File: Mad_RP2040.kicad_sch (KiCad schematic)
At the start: 22 parts, among them J1 USB_C_Receptacle, SW1 SW_SPST, SW2 SW_SPST, U0 PCB, U1 ECMF02-2AMX6

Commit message: BOM update
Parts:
- C1, C2: LCSC PN (none) -> C432917
- C3: LCSC PN (none) -> C472857
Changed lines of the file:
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@@
+			)
+		)
+		(property "LCSC PN" "C472857"
+			(at 104.14 39.37 0)
+			(effects
+				(font
+					(size 1.27 1.27)
+				)
+				(hide yes)
 			)
 		)
@@
 			)
 		)
+		(property "LCSC PN" "C432917"
+			(at 66.04 39.37 0)
+			(effects
+				(font
+					(size 1.27 1.27)
+				)
+				(hide yes)
+			)
+		)
 		(pin "2"
 		)
@@
 			(at 87.63 39.37 0)
 			(effects
+				(font
+					(size 1.27 1.27)
+				)
+				(hide yes)
+			)
+		)
+		(property "LCSC PN" "C432917"
+			(at 87.63 39.37 0)
+			(effects

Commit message: BOM consolidation
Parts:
- added D9: B5817WS, Diode_SMD:D_SOD-323, symbol Device:D_Schottky
- added F1: 500mA, Fuse:Fuse_0402_1005Metric, symbol Device:Polyfuse_Small
- C3: LCSC PN C472857 -> C2932476
- FB1: value BLM15PX330SN1D -> 33 Ohms Ferrite
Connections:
- net +5V: now also D9.1 (K); no longer FB1.2
- new net: D9.2 (A), F1.1
- new net: F1.2, FB1.2
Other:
- moved on the sheet: C2, C3

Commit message: BOM update
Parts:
- C1, C2: LCSC (none) -> C432917; LCSC PN C432917 -> (none)
- C3: LCSC (none) -> C2932476; LCSC PN C2932476 -> (none)
- D1, D2: LCSC (none) -> C435829; LCSC PN C435829 -> (none)
- D3, D4: LCSC (none) -> C5149201; LCSC PN C5149201 -> (none)
- D8: LCSC (none) -> C2886570; LCSC PN C2886570 -> (none)
- D9: LCSC (none) -> C122854; LCSC PN C122854 -> (none)
- F1: LCSC (none) -> C206938; LCSC PN C206938 -> (none)
- FB1, FB2: LCSC (none) -> C160974; LCSC PN C160974 -> (none)
- J1: LCSC (none) -> C3020560; LCSC PN C3020560 -> (none)
- R1, R2: LCSC (none) -> C105872; LCSC PN C105872 -> (none)
- SW1, SW2: LCSC (none) -> C2803348; LCSC PN C2803348 -> (none)
- U1: LCSC (none) -> C2651144; LCSC PN C2651144 -> (none)
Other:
- moved on the sheet: C2, C3, D9, F1

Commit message: Update todo's
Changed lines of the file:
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@@
-		)
-	)
-	(text_box "TODO:\n\n#* Cleanup bom, remove trailing spaces\n#* Get missing 3D models\n* Finish off PCB routing\n#* Check LED selection\n* BOM consolidation if possible\n#* Create template for page title block"
-		(exclude_from_sim no)
-		(at 151.765 -34.925 0)
-		(size 132.715 45.72)
-		(stroke
-			(width 0)
-			(type default)
-		)
-		(fill
-			(type none)
-		)
-		(effects
-			(font
-				(size 3 3)
-				(thickness 0.6)
-				(bold yes)
-			)
-			(justify left top)
 		)
 	)

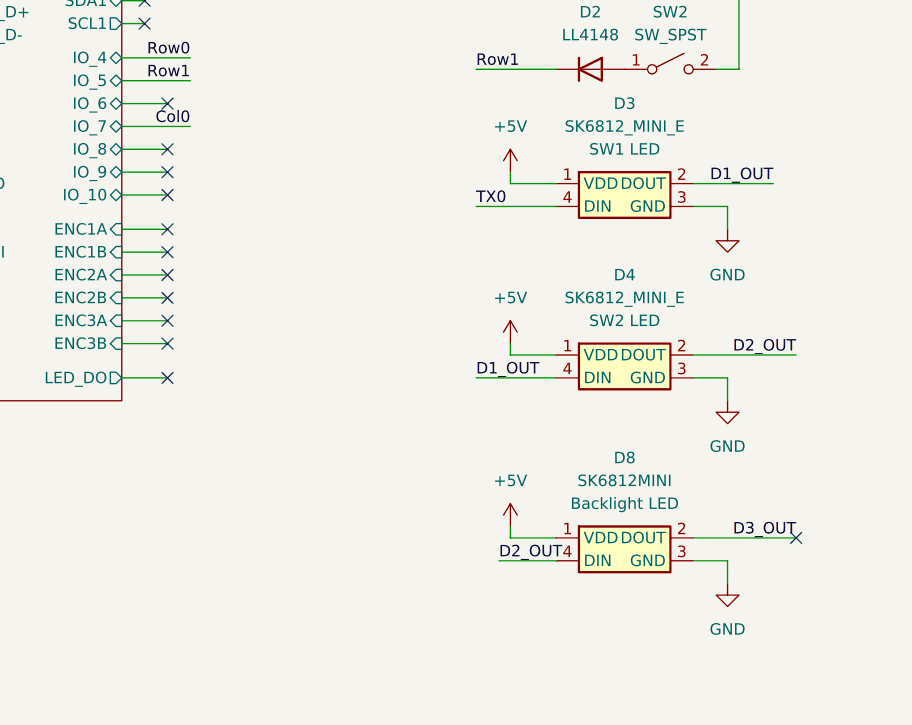
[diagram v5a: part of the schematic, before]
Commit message: Minor silk update
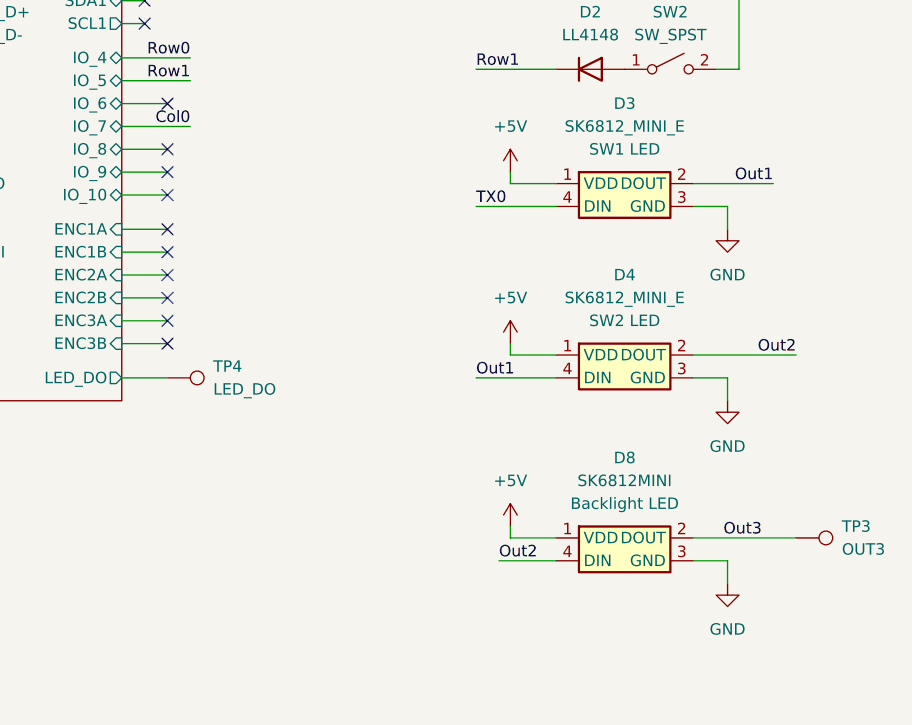
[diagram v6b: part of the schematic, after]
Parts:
- added TP3: OUT3, TestPoint:TestPoint_Pad_D1.0mm, symbol Connector:TestPoint
- added TP4: LED_DO, TestPoint:TestPoint_Pad_D1.0mm, symbol Connector:TestPoint
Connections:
- net RP2040/LED_DO: now also TP4.1
- net D1_OUT renamed Out1
- net D2_OUT renamed Out2
- net D3_OUT renamed Out3
- net Out3: now also TP3.1
- no-connect marks 26 -> 24

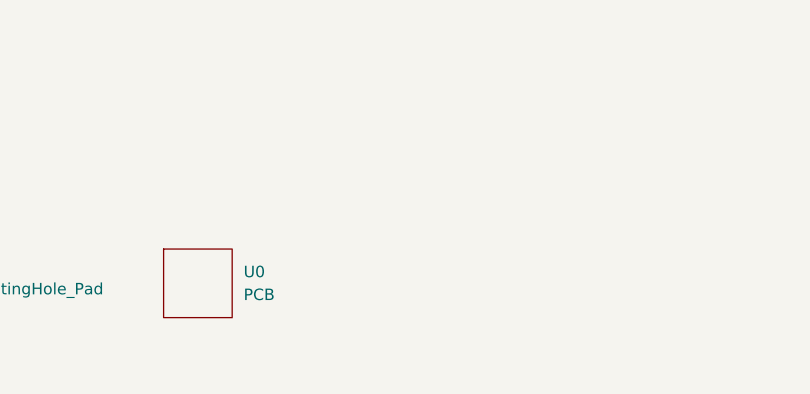
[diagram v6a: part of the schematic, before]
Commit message: Add board tabs
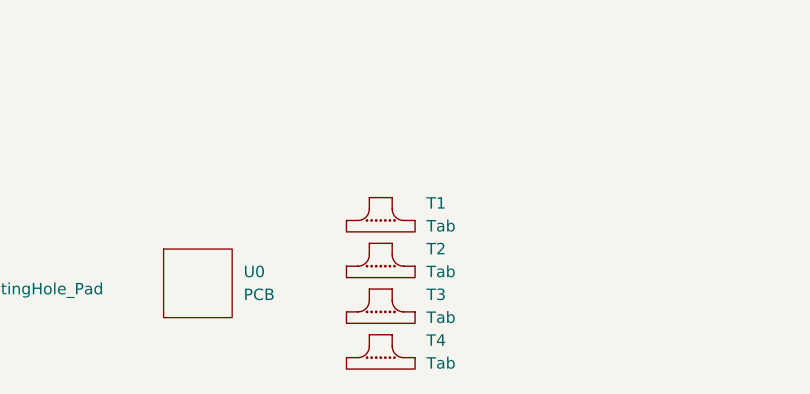
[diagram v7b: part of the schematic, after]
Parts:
- added T1, T2, T3, T4: Tab, PCM_kikit:Tab, symbol PCM_kikit:Tab

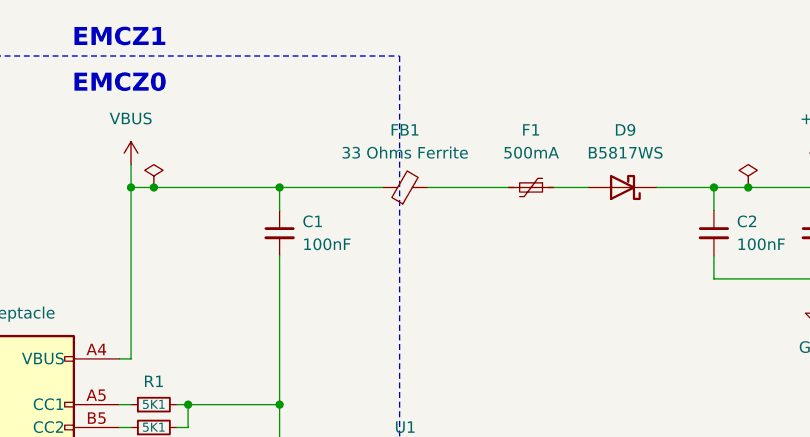
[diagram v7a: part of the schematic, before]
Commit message: Update value to mpn
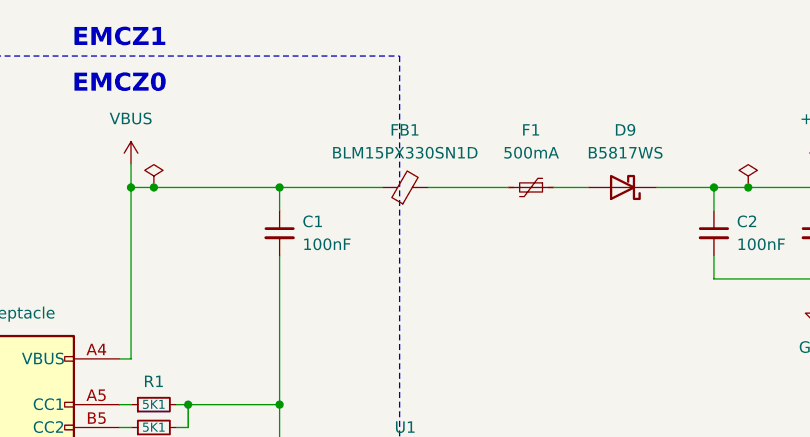
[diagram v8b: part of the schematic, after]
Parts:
- FB1: value 33 Ohms Ferrite -> BLM15PX330SN1D
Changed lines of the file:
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@@
 			)
 		)
-		(property "Value" "33 Ohms Ferrite"
+		(property "Value" "BLM15PX330SN1D"
 			(at 79.9719 30.48 90)
 			(effects
